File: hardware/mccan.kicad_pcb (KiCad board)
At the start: 8 copper layers, 200 x 140 mm, 238 parts, among them J1 PWR pigtail -> SS1.5 3w, J2 Prog/UART, J3 FL pigtail -> SS1.0 key A / b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, J4 FR pigtail -> SS1.0 key B / g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, J5 RL pigtail -> SS1.0 key C / b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, J6 RR pigtail -> SS1.0 key D / n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, J7 DENALI pigtail -> SS1.5 3w, J8 CAN pigtail -> SS1.0 2w, Q10 IPT008N06NM5LF, Q11 IPT008N06NM5LF, Q12 MMBT3904, Q2 MMBT3904, Q3 MMBT3904, Q4 NX5020UNBKS, Q5 NX5020UNBKS, Q6 NX5020UNBKS, Q7 NX5020UNBKS, Q8 NX5020UNBKS, Q9 NX5020UNBKS, SW1 BOOT, SW2 EN/RESET, U1 LM5164DDA, U10 LTC4380HMS-2, U2 LM5164DDA, U3 LM51571-Q1, U4 DML3017LDC, U5 ESP32-WROOM-32E-N8, U6 TJA1042T/3, U7 PCA9685PW/Q900, U8 ADG706, U9 BTS7008-2EPA

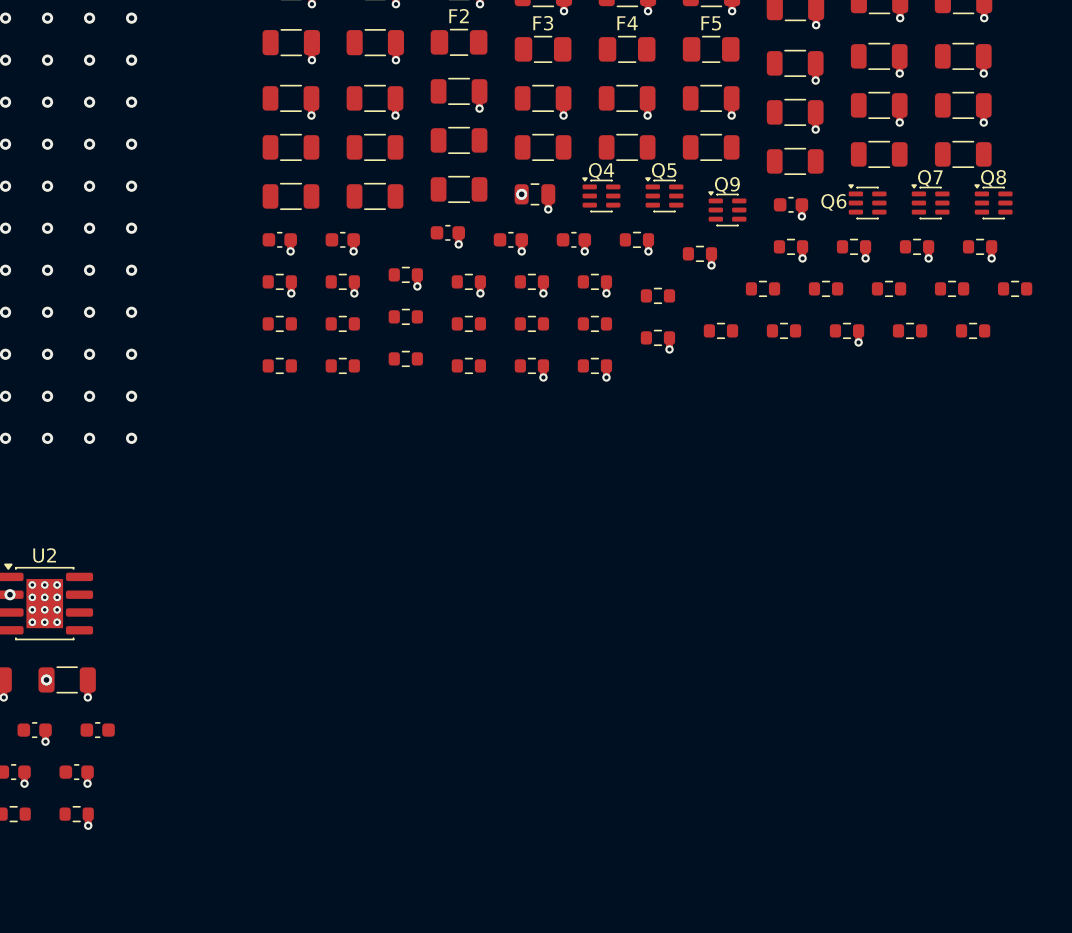
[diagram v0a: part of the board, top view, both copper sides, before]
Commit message: hw(pcb): fix round 3 (2/2) -- route the CAN haul as a true matched pair
The J8->L6 long haul (CANH/CANL) was not a matched differential pair:
CANH wove through 10 interior bends dodging 0.6 mm GND drop vias that
actually move out of the way on their own (gnd_drops() runs after
hand routes and calls via_ok() to refuse any drop that clashes with
hand copper), while CANL ran almost straight with 2 bends. Measured
centre-to-centre spacing ranged 1.027-4.600 mm.

Re-routed both tracks from a shared centreline (J8.1 (67.400,130.590)
-> L6.4 (193.575,31.300), 160.557 mm at 38.2 deg), each offset +-0.325
mm perpendicular to it for an exact constant 0.650 mm centre-to-
centre, fanning to pad pitch only in the last 1-2 mm at each end (J8
4.6 mm, L6 2.5 mm pitch), staying on In2.Cu throughout, and routed
straight through where GND drops previously sat instead of dodging
them.

One obstacle not named in the brief's corridor scan: L6.2's own via
(Net-(U6-CANL), part of the untouched transceiver leg) sits only
0.849 mm off the centreline, inside CANH's 0.325 mm offset. Fixed
with a local, CANH-only two-bend deviation in the last ~7 mm of the
approach to L6 (matched-pair section ends at t=154 mm along the
centreline; an added waypoint clears L6.1/L6.2/L6.3 by >=0.30 mm on
both new segments), leaving CANH with 3 interior bends against CANL's
2 rather than a symmetric 2-and-2. Treated as legitimate: it mirrors
the original design's own "(L6 approach, legitimate)" exception for
asymmetric approach-only bends, and the pair holds exact 0.650 mm
spacing everywhere else.

Before -> after (see task-8-fix-3-report.md for full detail):
  min c-to-c:    1.027 -> 0.646 mm
  max c-to-c:    4.600 -> 2.166 mm  (now confined to the two pad-pitch
                                      fan regions, not mid-haul)
  mean c-to-c:   2.388 -> 0.689 mm
  spread:        3.573 -> 1.520 mm
  CANH bends:    10 -> 3
  CANL bends:    2 -> 2
  CANH length: 160.626 mm, CANL length: 160.265 mm, diff 0.361 mm

gen_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
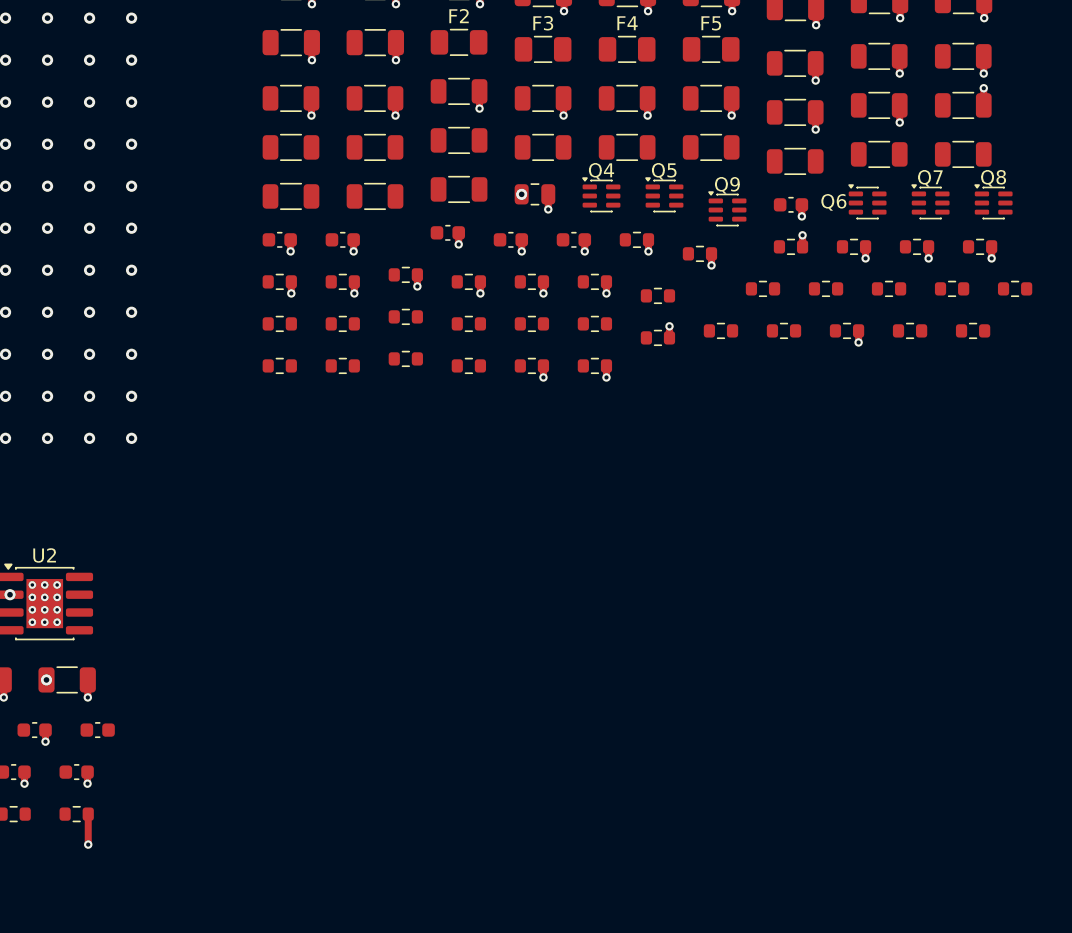
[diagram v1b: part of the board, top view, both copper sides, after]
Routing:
- net /CANL: track 174.4 -> 179.2 mm
- net GND: track 148.8 -> 150.2 mm
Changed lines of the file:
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@@
 	(segment
 		(start 67.4 130.59)
-		(end 108.4799 97.2453)
+		(end 68.7707 129.0978)
 		(width 0.3)
 		(layer "In2.Cu")
@@
 	)
 	(segment
-		(start 108.4799 97.2453)
-		(end 113.5269 93.2737)
+		(start 68.7707 129.0978)
+		(end 188.2209 35.0997)
 		(width 0.3)
 		(layer "In2.Cu")
@@
 	)
 	(segment
-		(start 113.5269 93.2737)
-		(end 149.4137 66.0515)
+		(start 188.2209 35.0997)
+		(end 189.58 34.48)
 		(width 0.3)
 		(layer "In2.Cu")
@@
 	)
 	(segment
-		(start 149.4137 66.0515)
-		(end 154.3646 62.1555)
+		(start 189.58 34.48)
+		(end 193.575 31.3)
 		(width 0.3)
 		(layer "In2.Cu")
@@
 	)
 	(segment
-		(start 154.3646 62.1555)
-		(end 162.5813 54.1626)
-		(width 0.3)
-		(layer "In2.Cu")
-		(net 5)
-	)
-	(segment
-		(start 162.5813 54.1626)
-		(end 167.0782 52.1509)
-		(width 0.3)
-		(layer "In2.Cu")
-		(net 5)
-	)
-	(segment
-		(start 167.0782 52.1509)
-		(end 172.4254 46.9251)
-		(width 0.3)
-		(layer "In2.Cu")
-		(net 5)
-	)
-	(segment
-		(start 172.4254 46.9251)
-		(end 177.4724 42.9535)
-		(width 0.3)
-		(layer "In2.Cu")
-		(net 5)
-	)
-	(segment
-		(start 177.4724 42.9535)
-		(end 187.5212 37.0818)
-		(width 0.3)
-		(layer "In2.Cu")
-		(net 5)
-	)
-	(segment
-		(start 187.5212 37.0818)
-		(end 192.5682 33.1102)
-		(width 0.3)
-		(layer "In2.Cu")
-		(net 5)
-	)
-	(segment
-		(start 192.5682 33.1102)
-		(end 193.575 31.3)
-		(width 0.3)
-		(layer "In2.Cu")
-		(net 5)
-	)
-	(segment
 		(start 72 130.59)
-		(end 164.0568 56.2779)
+		(end 69.1727 129.6086)
 		(width 0.3)
 		(layer "In2.Cu")
@@
 	)
 	(segment
-		(start 164.0568 56.2779)
-		(end 168.9198 52.4063)
+		(start 69.1727 129.6086)
+		(end 188.6229 35.6105)
 		(width 0.3)
 		(layer "In2.Cu")
@@
 	)
 	(segment
-		(start 168.9198 52.4063)
+		(start 188.6229 35.6105)
 		(end 193.575 33.8)
 		(width 0.3)
@@
 	)
 	(via
-		(at 111.905 95.655)
+		(at 111.905 97.005)
 		(size 0.6)
 		(drill 0.3)
@@
 	)
 	(via
-		(at 162.905 55.155)
+		(at 162.905 53.505)
 		(size 0.6)
 		(drill 0.3)
@@
 	)
 	(via
-		(at 175.8425 45.455)
+		(at 175.8425 43.005)
 		(size 0.6)
 		(drill 0.3)
@@
 	)
 	(via
-		(at 153.405 61.655)
+		(at 153.405 60.005)
 		(size 0.6)
 		(drill 0.3)
@@
 	(segment
 		(start 111.905 94.83)
-		(end 111.905 95.655)
+		(end 111.905 97.005)
 		(width 0.5)
 		(layer "F.Cu")
@@
 	(segment
 		(start 162.905 54.33)
-		(end 162.905 55.155)
+		(end 162.905 53.505)
 		(width 0.5)
 		(layer "F.Cu")
@@
 	(segment
 		(start 175.8425 44.23)
-		(end 175.8425 45.455)
+		(end 175.8425 43.005)
 		(width 0.5)
 		(layer "F.Cu")
@@
 	(segment
 		(start 153.405 60.83)
-		(end 153.405 61.655)
-		(width 0.5)
-		(layer "F.Cu")
+		(end 153.405 60.005)
+		(width 0.5)
+		(layer "F.Cu")

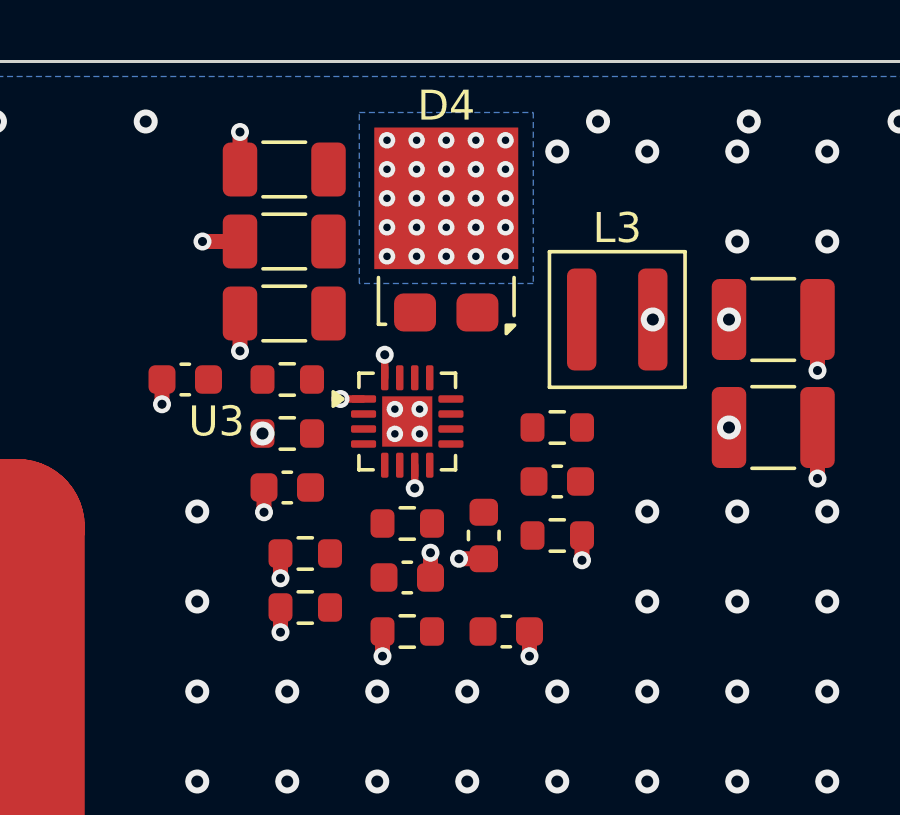
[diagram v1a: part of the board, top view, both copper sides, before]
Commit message: hw(pcb): the boost switch node, by hand and tight
The LM51571 integrates its switch, so there are no gate loops and this is the only
fast edge on the board; the boost is non-synchronous, so D4 is inside the
commutation loop. Loop area is a geometric property no router optimises for -- it
will hand back an electrically correct switch node that rings, and the failure shows
up on the bench rather than in any gate. Hence by hand.

The return half is deliberately not routed: In1.Cu is solid GND one 0.1 mm prepreg
below F.Cu, so the return mirrors the outbound path beneath it, which is smaller than
any trace. COMP and FB_24V are kept off SW; FB_24V taps the far end of the output cap
by reading through the +24V pour instead of hauling F.Cu round from the caps, per the
controller's ruling (R12.1/C61.1 drop straight to the pour).

Net-(U3-SS) is the one net that could not stay on F.Cu: it is boxed in by MODE, the
GND paddle and the FB_24V hop it has to cross to reach C25, so it ducks to In5.Cu for
5.8 mm to pass under the hop and the C24/R14 pair (SMD pads have no copper off F.Cu,
so the duck-under clears them for free) before returning to F.Cu.

PGND gets no new routes: the paddle's four thermal vias and the automatic per-pad GND
drops already connect everything this task touches. The VBAT feed into the boost was
already satisfied by a Task 7 via sitting exactly on L3.1's pad centre.

Loop area 13.23 mm2 (shoelace over the +24V bus/rung branch point (83.375, 24.5) ->
rung end at D4's tab (86.5, 24.5) -> D4/SW column start (86.5, 28.365) -> SW column
stop (86.5, 30.55) -> U3's GND paddle centre (86.0, 32.0) -> closed back to start).

Co-Authored-By: Claude Opus 5 <noreply@anthropic.com>
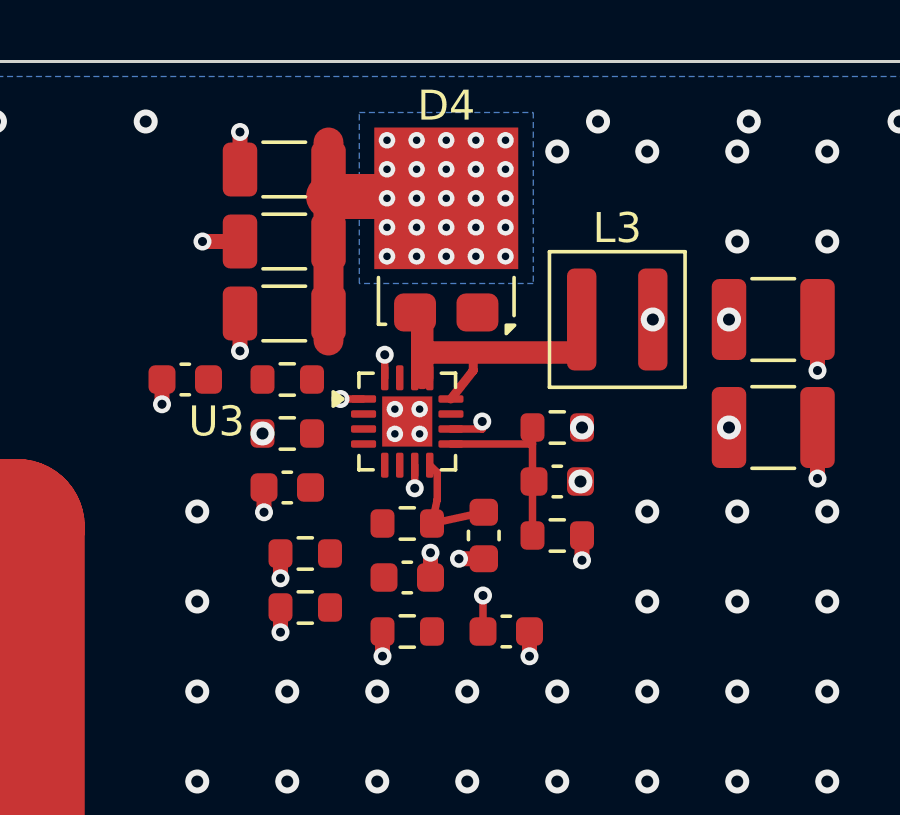
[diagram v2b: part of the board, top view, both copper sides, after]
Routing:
- net /+24V: track 0.00 -> 9.73 mm, vias 25 -> 27
- net /rails/SW_BOOST: track 0.00 -> 9.31 mm
- net Net-(U3-SS): track 0.00 -> 8.29 mm, vias 0 -> 2
- net /rails/FB_24V: track 0.00 -> 6.32 mm
- net Net-(U3-COMP): track 0.00 -> 3.83 mm
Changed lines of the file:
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@@
 		(net 145)
 	)
+	(segment
+		(start 86.5 28.365)
+		(end 86.5 30.55)
+		(width 0.75)
+		(layer "F.Cu")
+		(net 105)
+	)
+	(segment
+		(start 91.815 29.7)
+		(end 86.5 29.7)
+		(width 0.75)
+		(layer "F.Cu")
+		(net 105)
+	)
+	(segment
+		(start 87.4562 31.25)
+		(end 88.2 30.3)
+		(width 0.3)
+		(layer "F.Cu")
+		(net 105)
+	)
+	(segment
+		(start 88.2 30.3)
+		(end 88.2 29.7)
+		(width 0.3)
+		(layer "F.Cu")
+		(net 105)
+	)
+	(segment
+		(start 83.375 22.7)
+		(end 83.375 29.3)
+		(width 1)
+		(layer "F.Cu")
+		(net 4)
+	)
+	(segment
+		(start 83.375 24.5)
+		(end 86.5 24.5)
+		(width 1.5)
+		(layer "F.Cu")
+		(net 4)
+	)
+	(segment
+		(start 86.75 33.4562)
+		(end 87 33.7)
+		(width 0.25)
+		(layer "F.Cu")
+		(net 137)
+	)
+	(segment
+		(start 87 33.7)
+		(end 87 34.6)
+		(width 0.25)
+		(layer "F.Cu")
+		(net 137)
+	)
+	(segment
+		(start 87 34.6)
+		(end 86.825 35.4)
+		(width 0.25)
+		(layer "F.Cu")
+		(net 137)
+	)
+	(segment
+		(start 86.825 35.4)
+		(end 88.55 35.025)
+		(width 0.25)
+		(layer "F.Cu")
+		(net 137)
+	)
+	(segment
+		(start 87.4562 32.75)
+		(end 90.175 32.75)
+		(width 0.25)
+		(layer "F.Cu")
+		(net 102)
+	)
+	(segment
+		(start 90.175 32.2)
+		(end 90.175 35.8)
+		(width 0.25)
+		(layer "F.Cu")
+		(net 102)
+	)
+	(segment
+		(start 87.4562 32.25)
+		(end 88.5 32.25)
+		(width 0.25)
+		(layer "F.Cu")
+		(net 140)
+	)
+	(segment
+		(start 88.5 32.25)
+		(end 88.5 32)
+		(width 0.25)
+		(layer "F.Cu")
+		(net 140)
+	)
+	(segment
+		(start 88.5 32)
+		(end 88.525 37.8)
+		(width 0.25)
+		(layer "In5.Cu")
+		(net 140)
+	)
+	(segment
+		(start 88.525 37.8)
+		(end 88.525 39)
+		(width 0.25)
+		(layer "F.Cu")
+		(net 140)
+	)
 	(via
 		(at 37.9 48.7)
@@
 	)
 	(via
+		(at 91.825 32.2)
+		(size 0.8)
+		(drill 0.4)
+		(layers "F.Cu" "B.Cu")
+		(net 4)
+	)
+	(via
+		(at 91.775 34)
+		(size 0.8)
+		(drill 0.4)
+		(layers "F.Cu" "B.Cu")
+		(net 4)
+	)
+	(via
+		(at 88.5 32)
+		(size 0.6)
+		(drill 0.3)
+		(layers "F.Cu" "B.Cu")
+		(net 140)
+	)
+	(via
+		(at 88.525 37.8)
+		(size 0.6)
+		(drill 0.3)
+		(layers "F.Cu" "B.Cu")
+		(net 140)
+	)
+	(via
